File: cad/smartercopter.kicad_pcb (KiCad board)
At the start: 2 copper layers, 0 parts

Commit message: all components spread out on sheet
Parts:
- added A1: 2450AT42A100, hlib:2450AT42A100, F.Cu at (141.2, 144.0)
- added BT1: BATTERY, Pin_Headers:Pin_Header_Straight_1x02, F.Cu at (111.7, 144.2)
- added C1: 1uF, Capacitors_SMD:C_0402, F.Cu at (106.6, 81.1)
- added C10: 12pF, Capacitors_SMD:C_0201, F.Cu at (142.2, 123.0)
- added C11: 12pF, Capacitors_SMD:C_0201, F.Cu at (146.8, 123.0)
- added C12: DNM, Capacitors_SMD:C_0402, F.Cu at (114.3, 123.0)
- added C13: DNM, Capacitors_SMD:C_0402, F.Cu at (109.7, 123.0)
- added C14: 100nF, Capacitors_SMD:C_0402, F.Cu at (123.2, 101.4)
- added C15: 100nF, Capacitors_SMD:C_0402, F.Cu at (162.5, 101.4)
- added C16: 10nF, Capacitors_SMD:C_0402, F.Cu at (123.6, 123.0)
- added C17: 4.7uF, Capacitors_SMD:C_0603, F.Cu at (98.6, 101.6)
- added C18: 100nF, Capacitors_SMD:C_0402, F.Cu at (113.4, 101.4)
- added C19: 10nF, Capacitors_SMD:C_0402, F.Cu at (137.5, 123.0)
- added C2: 100nF, Capacitors_SMD:C_0402, F.Cu at (128.1, 101.4)
- added C20: 1uF, Capacitors_SMD:C_0402, F.Cu at (139.1, 81.1)
- added C21: 4.7uF, Capacitors_SMD:C_0603, F.Cu at (93.7, 101.6)
- added C22: 10nF, Capacitors_SMD:C_0402, F.Cu at (132.9, 123.0)
- added C23: 10nF, Capacitors_SMD:C_0402, F.Cu at (128.2, 123.0)
- added C24: 22pF, Capacitors_SMD:C_0402, F.Cu at (118.9, 123.0)
- added C25: 22pF, Capacitors_SMD:C_0402, F.Cu at (151.4, 123.0)
- added C26: 4.7uF, Capacitors_SMD:C_0603, F.Cu at (88.8, 101.6)
- added C27: 4.7uF, Capacitors_SMD:C_0603, F.Cu at (83.9, 101.6)
- added C28: 100nF, Capacitors_SMD:C_0402, F.Cu at (133.0, 101.4)
- added C29: 100nF, Capacitors_SMD:C_0402, F.Cu at (157.6, 101.4)
- added C3: 100nF, Capacitors_SMD:C_0402, F.Cu at (147.7, 101.4)
- added C4: 100nF, Capacitors_SMD:C_0402, F.Cu at (152.6, 101.4)
- added C5: 100nF, Capacitors_SMD:C_0402, F.Cu at (142.8, 101.4)
- added C6: 100nF, Capacitors_SMD:C_0402, F.Cu at (137.9, 101.4)
- added C7: 220pF, Capacitors_SMD:C_0402, F.Cu at (118.3, 101.4)
- added C8: 1uF, Capacitors_SMD:C_0402, F.Cu at (101.9, 81.1)
- added C9: 1nF, Capacitors_SMD:C_0402, F.Cu at (97.3, 81.1)
- added D1: BI_COLOR_LED, hlib:APTB1612ESGC-F01, F.Cu at (136.3, 144.0)
- added D2: 2.7v, hlib:SOD-323, F.Cu at (82.3, 143.2)
- added D3: BAT54C, Diodes_SMD:Diode_SOT23, F.Cu at (116.7, 146.0)
- added D5: BAT54C, Diodes_SMD:Diode_SOT23, F.Cu at (121.6, 146.0)
- added FL1: 2450BM15A0002, hlib:2450BM15A0002, F.Cu at (152.4, 142.2)
- added P1: CONN_5, Pin_Arrays:pin_array_1x05, F.Cu at (181.6, 134.6)
- added P2: CONN_2, Pin_Headers:Pin_Header_Straight_1x02, F.Cu at (106.8, 144.2)
- added P3: CONN_2, Pin_Headers:Pin_Header_Straight_1x02, F.Cu at (101.9, 144.2)
- added P4: CONN_2, Pin_Headers:Pin_Header_Straight_1x02, F.Cu at (97.0, 142.9)
- added Q1: SiA910EDJ, hlib:SC-70-6L, F.Cu at (126.5, 144.5)
- added R1: 1K, Resistors_SMD:R_0402, F.Cu at (88.0, 81.2)
- added R10: 100k, Resistors_SMD:R_0402, F.Cu at (160.7, 123.1)
- added R11: 10, Resistors_SMD:R_0402, F.Cu at (95.7, 121.8)
- added R12: 36k, Resistors_SMD:R_0402, F.Cu at (162.3, 81.2)
- added R13: 62k, Resistors_SMD:R_0402, F.Cu at (100.4, 121.8)
- added R14: 0, Resistors_SMD:R_0402, F.Cu at (157.6, 81.2)
- added R15: 0, Resistors_SMD:R_0402, F.Cu at (143.7, 81.2)
- added R16: 39k, Resistors_SMD:R_0402, F.Cu at (153.0, 81.2)
- added R17: 30k, Resistors_SMD:R_0402, F.Cu at (91.1, 121.8)
- added R18: 39k, Resistors_SMD:R_0402, F.Cu at (105.0, 121.8)
- added R19: 30k, Resistors_SMD:R_0402, F.Cu at (81.8, 121.8)
- added R2: 1K, Resistors_SMD:R_0402, F.Cu at (83.4, 81.2)
- added R20: 100, Resistors_SMD:R_0402, F.Cu at (86.5, 121.8)
- added R21: 100k, Resistors_SMD:R_0402, F.Cu at (156.1, 123.1)
- added R22: 100, Resistors_SMD:R_0402, F.Cu at (148.3, 81.2)
- added R23: 100k, Resistors_SMD:R_0402, F.Cu at (79.0, 101.5)
- added R3: 2k7, Resistors_SMD:R_0402, F.Cu at (111.2, 81.2)
- added R4: 2k2, Resistors_SMD:R_0402, F.Cu at (129.8, 81.2)
- added R5: 2k2, Resistors_SMD:R_0402, F.Cu at (120.5, 81.2)
- added R6: 56k, Resistors_SMD:R_0402, F.Cu at (134.4, 81.2)
- added R7: 0, Resistors_SMD:R_0402, F.Cu at (92.7, 81.2)
- added R8: 2k2, Resistors_SMD:R_0402, F.Cu at (115.9, 81.2)
- added R9: 20k, Resistors_SMD:R_0402, F.Cu at (125.1, 81.2)
- added SW1: SW_PUSH_4, hlib:PTS840GMSMTRLFS, F.Cu at (131.4, 144.8)
- added U1: CC2541, SMD_Packages:LFCSP-40-1EP, F.Cu at (168.9, 144.8)
- added U2: MPU-9250, SMD_Packages:QFN-28-1EP, F.Cu at (78.7, 77.5)
- added U3: TPS73001, SMD_Packages:SOT-23-6, F.Cu at (103.2, 100.6)
- added U4: TPS73001, SMD_Packages:SOT-23-6, F.Cu at (108.1, 100.6)
- added U5: DRV8837, SMD_Packages:WSON-8-1EP, F.Cu at (87.3, 142.8)
- added X1: 32Mhz, hlib:4-SMD, F.Cu at (92.1, 143.0)

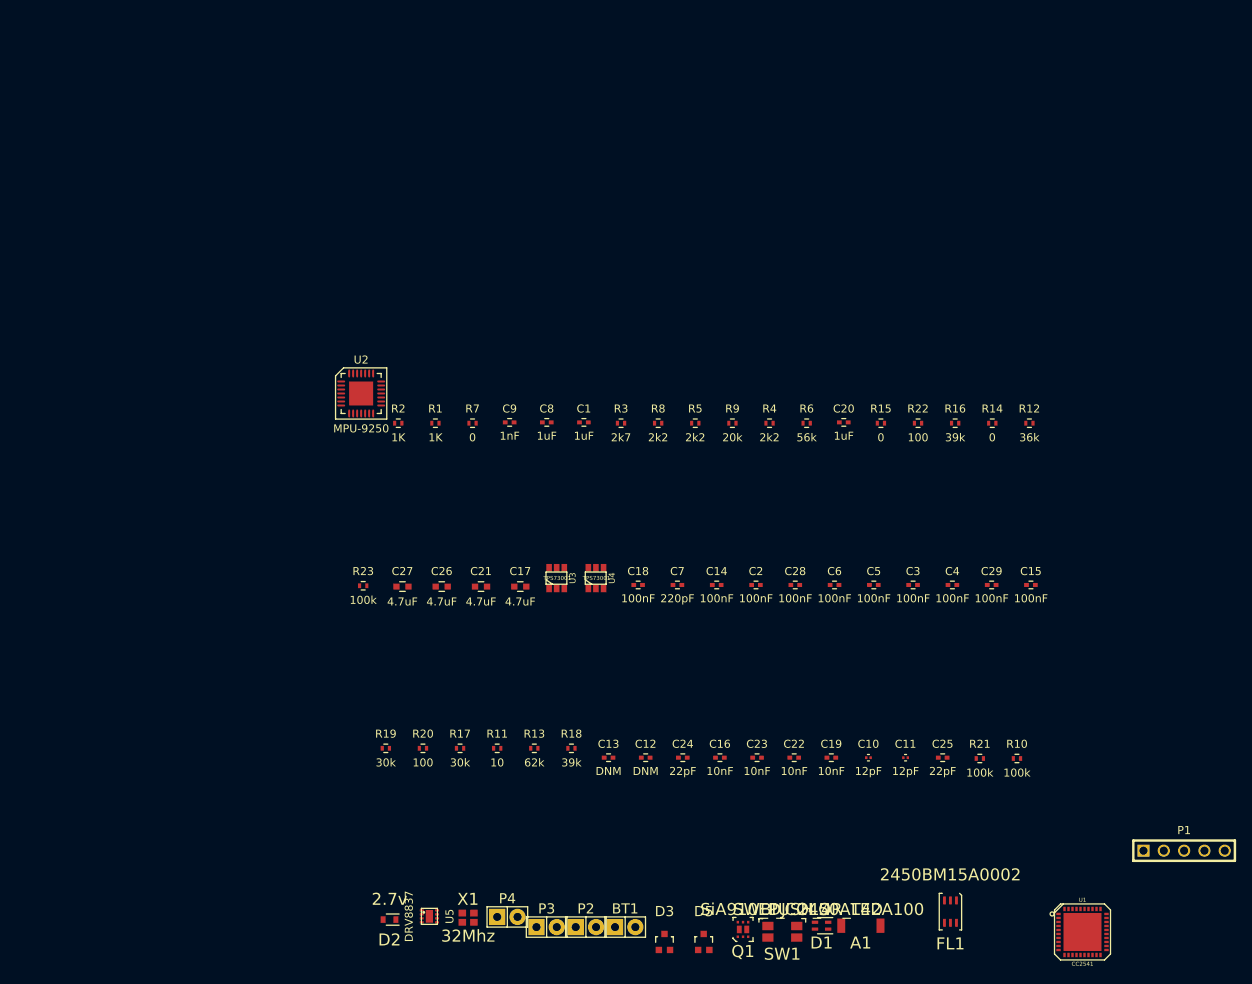
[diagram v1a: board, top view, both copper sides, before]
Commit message: found out decoupling caps are not connected in the net
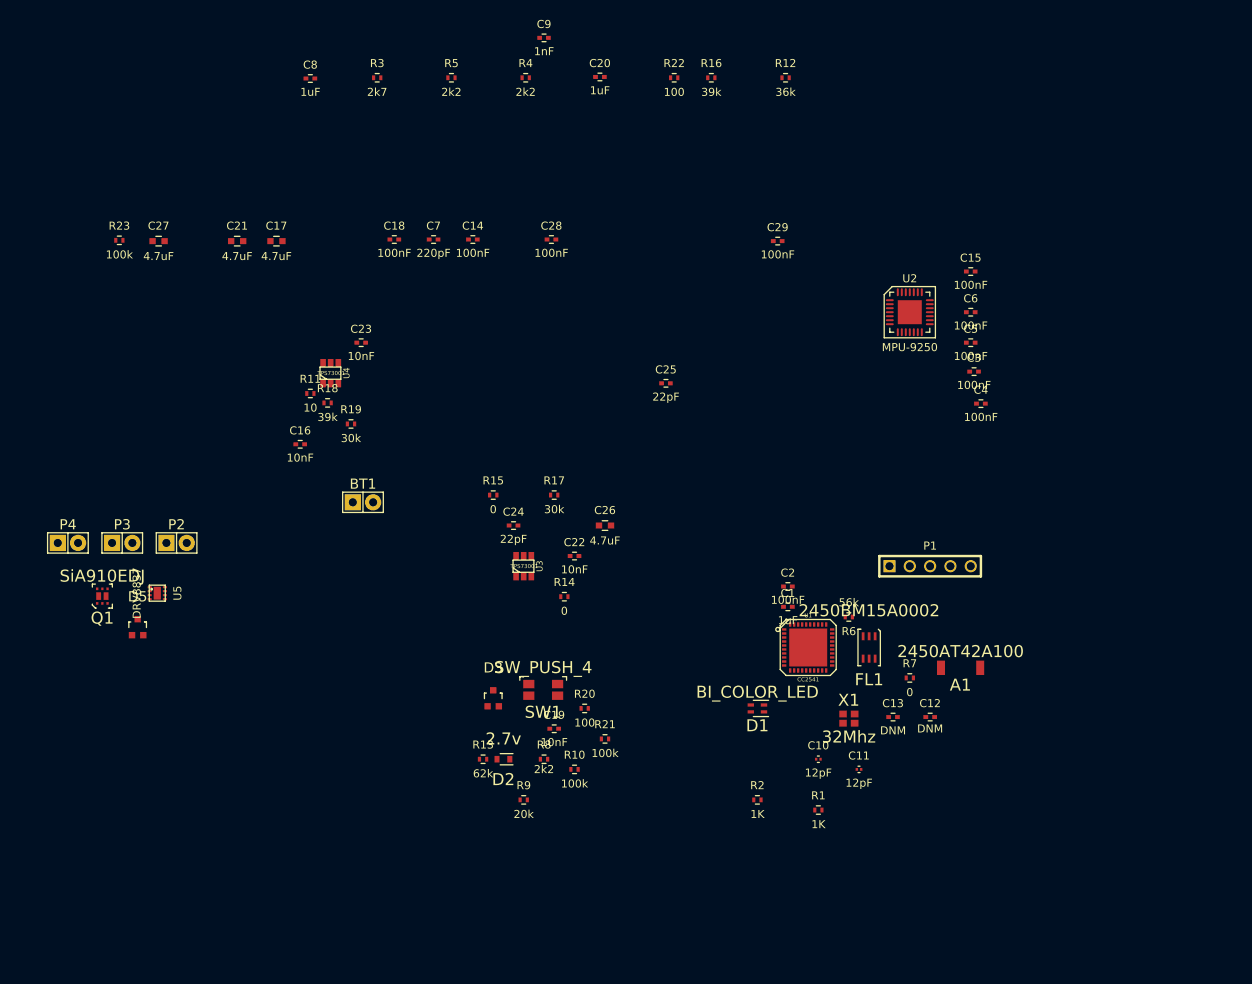
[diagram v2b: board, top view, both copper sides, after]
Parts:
- moved Q1 90.3 mm to (46.4, 102.8)
- moved D5 81.0 mm to (50.8, 106.7)
- moved P4 72.1 mm to (42.1, 96.2)
- moved C23 71.7 mm to (78.7, 71.1)
- moved P3 71.6 mm to (48.9, 96.2)
- moved P2 70.2 mm to (55.7, 96.2)
- moved U2 69.3 mm to (147.3, 67.3)
- moved R1 68.0 mm to (135.9, 129.5)
- moved C16 65.5 mm to (71.1, 83.8)
- moved R2 65.1 mm to (128.3, 128.3)
- moved R7 63.3 mm to (147.3, 113.0)
- moved BT1 62.4 mm to (79.0, 91.1)
- moved C25 58.2 mm to (116.8, 76.2)
- moved R14 57.7 mm to (104.1, 102.9)
- moved R10 55.3 mm to (105.4, 124.5)
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
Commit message: arranged stuff into smaller groups
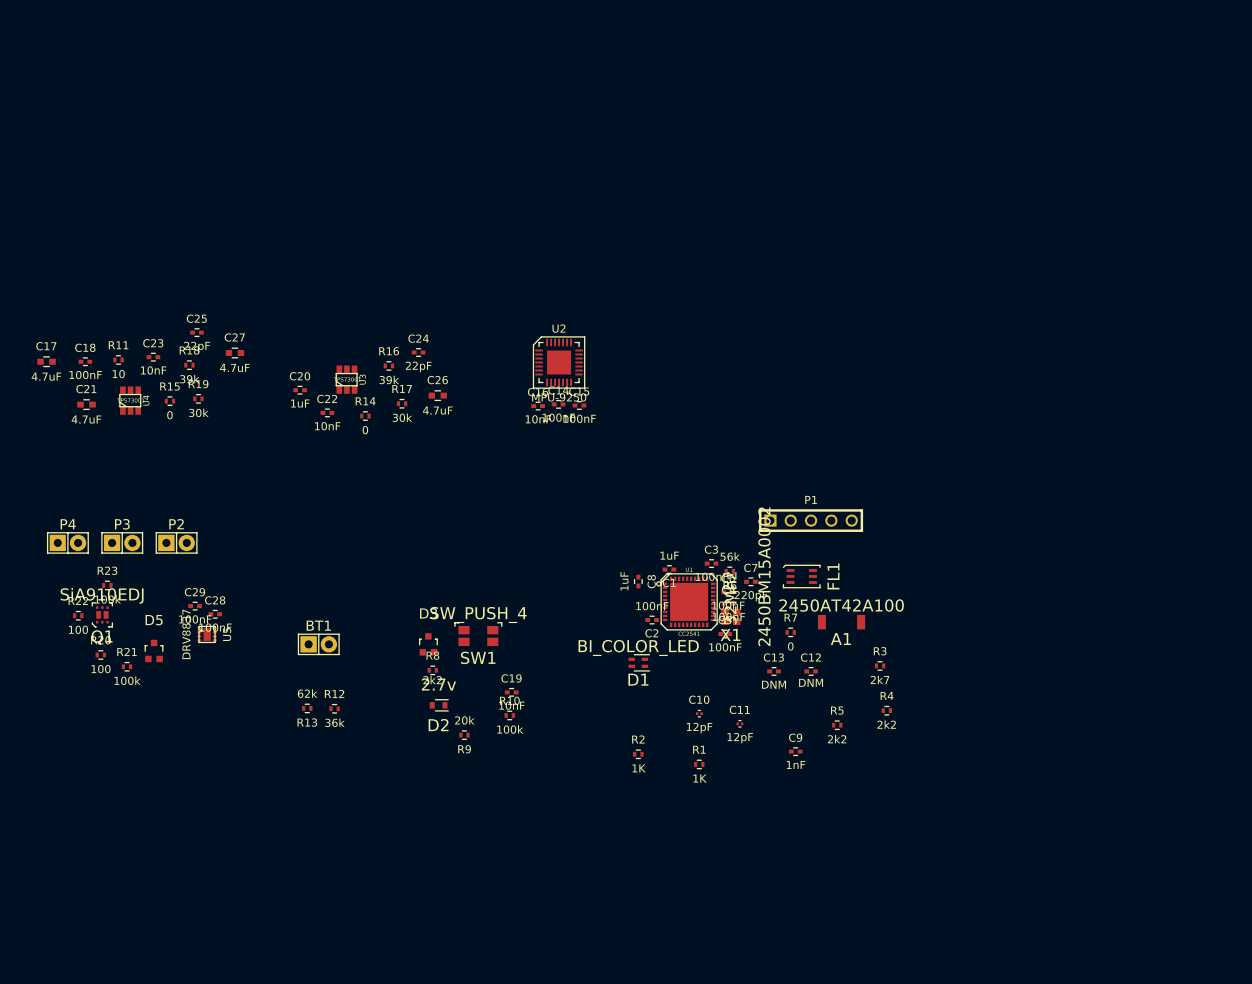
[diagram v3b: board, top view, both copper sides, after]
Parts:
- moved R22 100.4 mm to (43.4, 105.2)
- moved R12 96.9 mm to (75.4, 116.9)
- moved R3 96.7 mm to (143.6, 111.5)
- moved C9 94.6 mm to (133.1, 122.2)
- moved R5 94.2 mm to (138.2, 118.9)
- moved R4 91.1 mm to (144.4, 117.1)
- moved C29 85.9 mm to (58.0, 104.0)
- moved C8 75.1 mm to (113.4, 101.0), turned to 270 degrees
- moved C28 62.9 mm to (60.5, 105.1)
- moved R20 60.8 mm to (46.2, 110.2)
- moved R21 60.4 mm to (49.5, 111.6)
- moved C25 59.0 mm to (58.2, 69.9)
- moved C7 58.3 mm to (127.5, 101.0)
- moved C20 54.2 mm to (71.1, 77.1)
- moved R16 54.1 mm to (82.2, 74.0)
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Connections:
- A1 pad 2: (no net) -> Net-(A1-Pad2)
- C1 pad 1: Net-(C1-Pad1) -> VCC
- C2 pad 1: Net-(C1-Pad1) -> VCC
- C3 pad 1: Net-(C3-Pad1) -> VCCA
- C4 pad 1: Net-(C3-Pad1) -> VCCA
- C5 pad 1: Net-(C3-Pad1) -> VCCA
- C6 pad 1: Net-(C3-Pad1) -> VCCA
- C7 pad 1: Net-(C3-Pad1) -> VCCA
- U1 pad 41: (no net) -> DGND

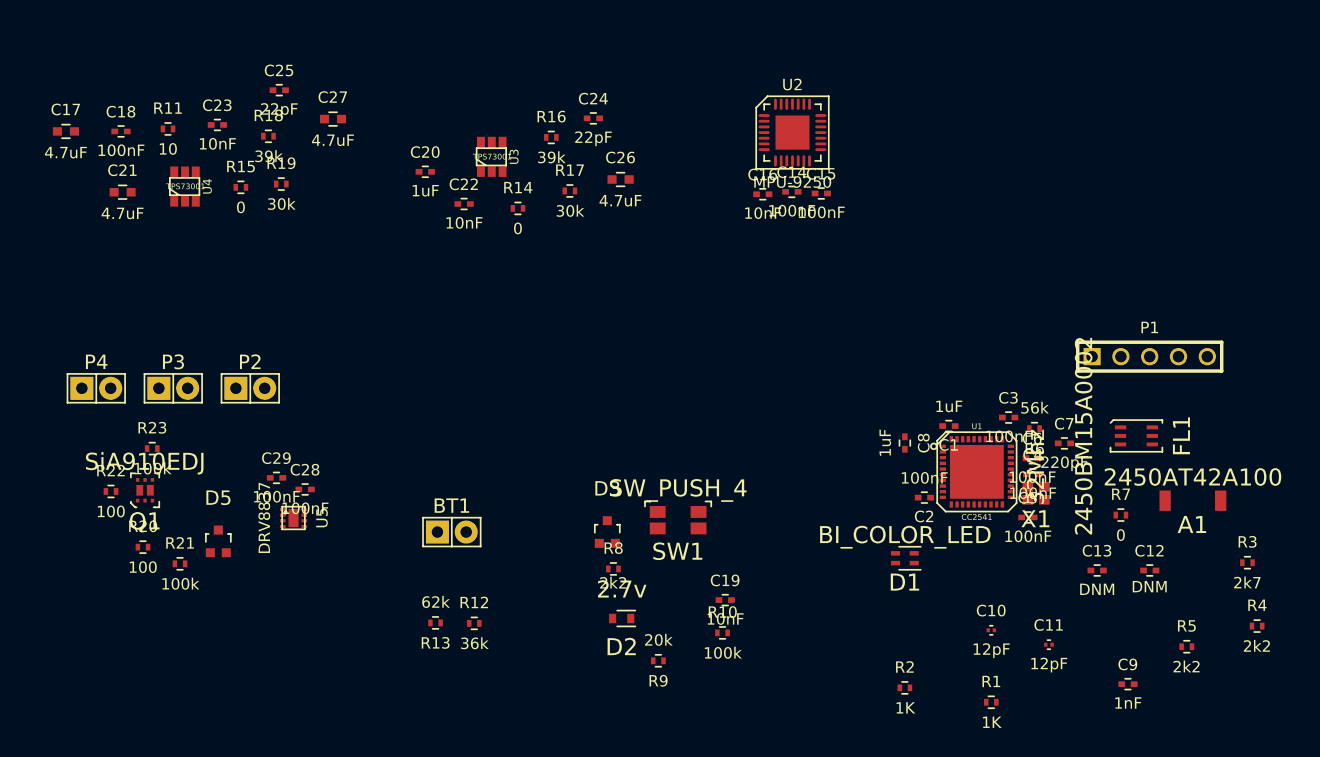
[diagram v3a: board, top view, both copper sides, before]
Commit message: components packed closer
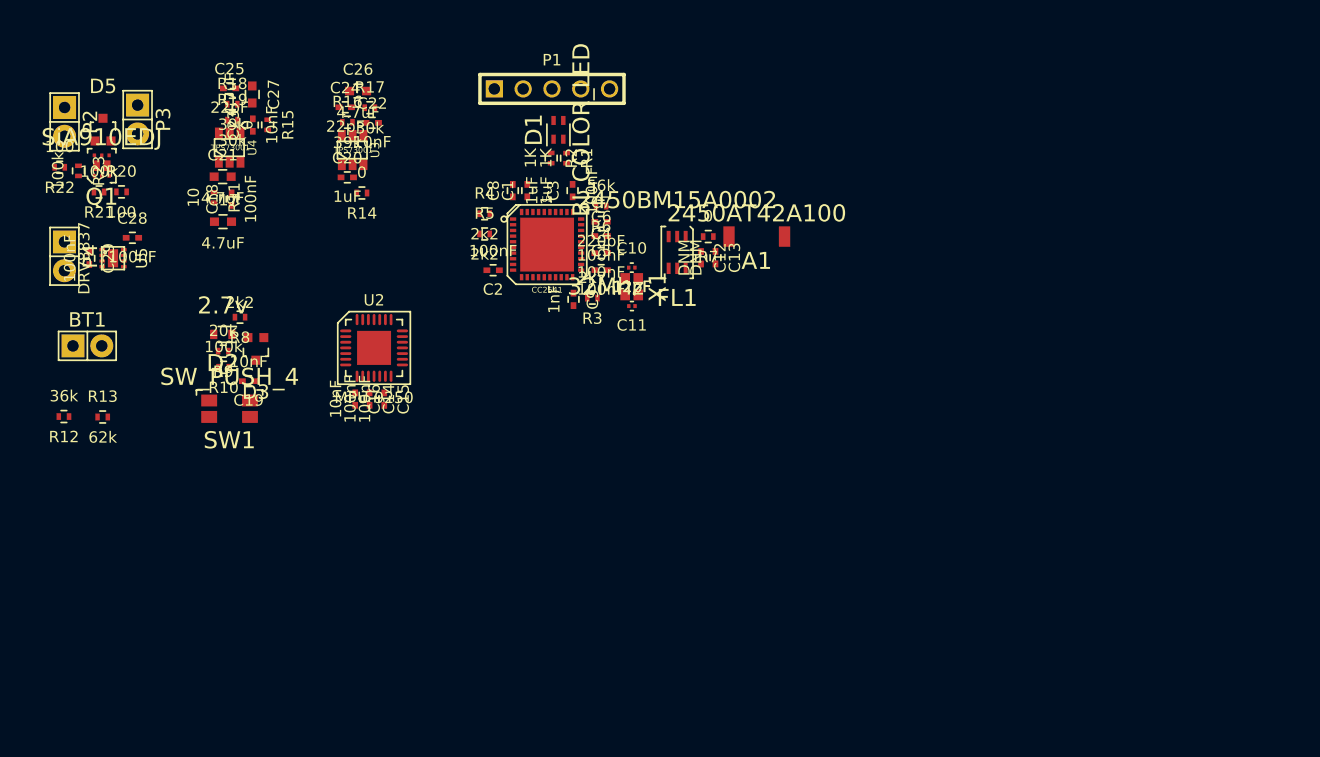
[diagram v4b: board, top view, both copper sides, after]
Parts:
- moved R4 77.2 mm to (76.3, 80.8)
- moved R5 71.8 mm to (76.3, 82.5)
- moved R3 62.3 mm to (85.8, 88.2), turned to 180 degrees
- moved R1 60.9 mm to (83.6, 75.9), turned to 270 degrees
- moved C9 59.5 mm to (84.2, 88.3), turned to 270 degrees
- moved P1 57.8 mm to (82.3, 69.8)
- moved R2 56.2 mm to (82.2, 75.8), turned to 270 degrees
- moved R10 49.8 mm to (53.3, 94.3), turned to 180 degrees
- moved D1 48.6 mm to (82.8, 73.4), turned to 270 degrees
- moved C12 48.2 mm to (95.4, 84.6), turned to 270 degrees
- moved C11 47.4 mm to (89.3, 88.9), turned to 180 degrees
- moved R9 47.1 mm to (53.3, 92.9)
- moved C19 46.3 mm to (55.5, 95.5), turned to 180 degrees
- moved C7 45.3 mm to (86.6, 81.5)
- moved C10 45.0 mm to (89.3, 85.5)
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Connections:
- U1 pad 32: /LED2 -> /LED1
- U1 pad 33: /LED1 -> /LED2

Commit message: board outline
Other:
- board outline added: 37.7 x 16.8 mm
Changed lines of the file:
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@@
     (area 0 0 0 0)
     (thickness 1.6)
-    (drawings 0)
+    (drawings 4)
     (tracks 0)
     (zones 0)
@@
       (net 4 DGND))
   )
+  (gr_line (start 150.8 83.8) (end 113.1 83.8) (layer Edge.Cuts) (width 0.1))
+  (gr_line (start 150.8 67.04) (end 150.8 83.8) (layer Edge.Cuts) (width 0.1))
+  (gr_line (start 113.1 67.04) (end 150.8 67.04) (layer Edge.Cuts) (width 0.1))
+  (gr_line (start 113.1 83.8) (end 113.1 67.04) (layer Edge.Cuts) (width 0.1))
 )
